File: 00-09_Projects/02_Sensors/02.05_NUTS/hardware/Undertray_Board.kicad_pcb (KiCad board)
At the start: 4 copper layers, 39.6 x 47.7 mm, 95 parts, among them J1 USB_C_Receptacle_USB2.0_16P, J2 Conn_01x04_Socket, J3 Conn_01x06_Pin, J4 SHF-107-01-L-D-SM, SW1 450404015514, SW2 TL3301EF160QG, U1 SN65HVD230, U2 AP2210K-3.3TRG1, U3 STM32F302C8Tx, U4 74HC2G32DP, U5 ASM330LHBTR, U6 VL53L4CDV0DH/1, Y1 RH100-16.000-9-1010-TR

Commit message: LED labels
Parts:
- added kibuzzard-6AD3F554: G***, kibuzzard-6AD3F554, F.Cu at (133.8, 74.9)
- added kibuzzard-6AD3F574: G***, kibuzzard-6AD3F574, F.Cu at (134.2, 80.6)
- added kibuzzard-6AD3F58A: G***, kibuzzard-6AD3F58A, F.Cu at (156.3, 56.8)
- added kibuzzard-6AD3F6DB: G***, kibuzzard-6AD3F6DB, F.Cu at (131.5, 77.6)

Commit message: extra changes
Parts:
- removed kibuzzard-6AD3F554: G***, kibuzzard-6AD3F554
- removed kibuzzard-6AD3F574: G***, kibuzzard-6AD3F574
- removed kibuzzard-6AD3F58A: G***, kibuzzard-6AD3F58A
- removed kibuzzard-6AD3F6DB: G***, kibuzzard-6AD3F6DB
- added C23: 0.1uF, Capacitor_SMD:C_0603_1608Metric_Pad1.08x0.95mm_HandSolder, F.Cu at (139.6, 82.8)
- added R19: 47k, Resistor_SMD:R_0402_1005Metric_Pad0.72x0.64mm_HandSolder, F.Cu at (141.8, 81.6)
- moved C16 3.98 mm to (135.9, 82.0), turned to 180 degrees
- moved D7 2.53 mm to (133.6, 82.9)
- moved R8 2.08 mm to (135.9, 83.6), turned to 180 degrees
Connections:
- U4 pad 2: BOOT0_TRIG -> Net-(C23-Pad1)
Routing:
- net Net-(C23-Pad1): track 0.00 -> 3.39 mm
- net BOOT0_SW: track 3.21 -> 5.41 mm
- net GND: track 32.8 -> 34.8 mm, vias 45 -> 44
- net Net-(D7-K): track 4.47 -> 6.12 mm
- net BOOT0_TRIG: track 9.74 -> 10.5 mm

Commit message: extra changes
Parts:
- R10, R5, R6, R9: value 220 -> 330
- R12: value 100 -> 200
- R13, R16: value 22 -> 47
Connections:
- J4 pad 08: SWO -> unconnected-(J4-Pad08)
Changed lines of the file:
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@@
 			)
 		)
-		(property "Value" "220"
+		(property "Value" "330"
 			(at 0 1.43 0)
 			(layer "F.Fab")
@@
 			)
 		)
-		(property "Value" "220"
+		(property "Value" "330"
 			(at 0 1.43 0)
 			(layer "F.Fab")
@@
 		(sheetname "/MCU/")
 		(sheetfile "mcu.kicad_sch")
+		(units
+			(unit
+				(name "A")
+				(pins "2" "4" "5" "6" "7" "3" "1")
+			)
+		)
 		(attr smd)
 		(duplicate_pad_numbers_are_jumpers no)
@@
 			)
 		)
-		(property "Value" "22"
+		(property "Value" "47"
 			(at 0 1.43 0)
 			(layer "F.Fab")
@@
 			(size 0.74 2.795)
 			(layers "F.Cu" "F.Mask" "F.Paste")
-			(net "SWO")
+			(net "unconnected-(J4-Pad08)")
 			(pinfunction "08_08")
-			(pintype "passive")
+			(pintype "passive+no_connect")
 			(solder_mask_margin 0.102)
 		)
@@
 			)
 		)
-		(property "Value" "22"
+		(property "Value" "47"
 			(at 0 1.43 0)
 			(layer "F.Fab")
@@
 			)
 		)
-		(property "Value" "220"
+		(property "Value" "330"
 			(at 0 1.43 0)
 			(layer "F.Fab")
@@
 			)
 		)
-		(property "Value" "220"
+		(property "Value" "330"
 			(at 0 1.43 90)
 			(layer "F.Fab")
@@
 			)
 		)
-		(property "Value" "100"
+		(property "Value" "200"
 			(at 0 1.43 0)
 			(layer "F.Fab")
@@
 	)
 	(segment
+		(start 140.475 80.8725)
+		(end 141.2025 81.6)
+		(width 0.3)
+		(layer "F.Cu")
+		(net "Net-(C23-Pad1)")
+	)
+	(segment
+		(start 140.865 81.9375)
+		(end 141.2025 81.6)
+		(width 0.3)
+		(layer "F.Cu")
+		(net "Net-(C23-Pad1)")
+	)
+	(segment
+		(start 139.6 81.9375)
+		(end 140.865 81.9375)
+		(width 0.3)
+		(layer "F.Cu")
+		(net "Net-(C23-Pad1)")
+	)
+	(segment
+		(start 140.475 80.25)
+		(end 140.475 80.8725)
+		(width 0.3)
+		(layer "F.Cu")
+		(net "Net-(C23-Pad1)")
+	)
+	(segment
 		(start 136.8 82)
 		(end 138.55 80.25)
@@
 		(net "Net-(U2-BYP{slash}ADJ)")
 	)
-	(segment
-		(start 140.475 80.8725)
-		(end 141.2025 81.6)
-		(width 0.3)
-		(layer "F.Cu")
-		(net "Net-(C23-Pad1)")
-	)
-	(segment
-		(start 140.865 81.9375)
-		(end 141.2025 81.6)
-		(width 0.3)
-		(layer "F.Cu")
-		(net "Net-(C23-Pad1)")
-	)
-	(segment
-		(start 139.6 81.9375)
-		(end 140.865 81.9375)
-		(width 0.3)
-		(layer "F.Cu")
-		(net "Net-(C23-Pad1)")
-	)
-	(segment
-		(start 140.475 80.25)
-		(end 140.475 80.8725)
-		(width 0.3)
-		(layer "F.Cu")
-		(net "Net-(C23-Pad1)")
-	)
 	(zone

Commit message: solder jumper for reset
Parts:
- added JP3: SolderJumper_2_Open, Jumper:SolderJumper-2_P1.3mm_Open_TrianglePad1.0x1.5mm, F.Cu at (130.8, 77.8)
- D3: value RB520S30T5G -> SDM20U30-7
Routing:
- net BOOT0: track 11.2 -> 18.8 mm
- net BOOT0_SW: track 5.41 -> 12.8 mm
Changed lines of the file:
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@@
 		(tags "resistor handsolder")
 		(property "Reference" "R5"
-			(at -0.025 1.5 0)
+			(at 2.7875 0 0)
 			(layer "F.SilkS")
 			(effects
@@
 		)
 	)
+	(footprint "Jumper:SolderJumper-2_P1.3mm_Open_TrianglePad1.0x1.5mm"
+		(layer "F.Cu")
+		(at 130.8 77.775 -90)
+		(descr "SMD Solder Jumper, 1x1.5mm Triangular Pads, 0.3mm gap, open")
+		(tags "solder jumper open")
+		(property "Reference" "JP3"
+			(at -0.775 -2 90)
+			(layer "F.SilkS")
+			(effects
+				(font
+					(size 1 1)
+					(thickness 0.15)
+				)
+			)
+		)
+		(property "Value" "SolderJumper_2_Open"
+			(at 0 1.9 90)
+			(layer "F.Fab")
+			(effects
+				(font
+					(size 1 1)
+					(thickness 0.15)
+				)
+			)
+		)
+		(property "Datasheet" ""
+			(at 0 0 270)
+			(unlocked yes)
+			(layer "F.Fab")
+			(hide yes)
+			(effects
+				(font
+					(size 1.27 1.27)
+					(thickness 0.15)
+				)
+			)
+		)
+		(property "Description" "Solder Jumper, 2-pole, open"
+			(at 0 0 270)
+			(unlocked yes)
+			(layer "F.Fab")
+			(hide yes)
+			(effects
+				(font
+					(size 1.27 1.27)
+					(thickness 0.15)
+				)
+			)
+		)
+		(property ki_fp_filters "SolderJumper*Open*")
+		(sheetname "/MCU/")
+		(sheetfile "mcu.kicad_sch")
+		(units
+			(unit
+				(name "A")
+				(pins "1" "2")
+			)
+		)
+		(zone_connect 1)
+		(attr exclude_from_bom allow_soldermask_bridges)
+		(duplicate_pad_numbers_are_jumpers no)
+		(fp_rect
+			(start -1.225 -0.75)
+			(end 1.225 0.75)
+			(stroke
+				(width 0)
+				(type default)
+			)
+			(fill yes)
+			(layer "F.Mask")
+		)
+		(fp_line
+			(start -1.4 1)
+			(end -1.4 -1)
+			(stroke
+				(width 0.12)
+				(type solid)
+			)
+			(layer "F.SilkS")
+		)
+		(fp_line
+			(start 1.4 1)
+			(end -1.4 1)
+			(stroke
+				(width 0.12)
+				(type solid)
+			)
+			(layer "F.SilkS")
+		)
+		(fp_line
+			(start -1.4 -1)
+			(end 1.4 -1)
+			(stroke
+				(width 0.12)
+				(type solid)
+			)
+			(layer "F.SilkS")
+		)
+		(fp_line
+			(start 1.4 -1)
+			(end 1.4 1)
+			(stroke
+				(width 0.12)
+				(type solid)
+			)
+			(layer "F.SilkS")
+		)
+		(fp_line
+			(start 1.65 1.25)
+			(end -1.65 1.25)
+			(stroke
+				(width 0.05)
+				(type solid)
+			)
+			(layer "F.CrtYd")
+		)
+		(fp_line
+			(start 1.65 1.25)
+			(end 1.65 -1.25)
+			(stroke
+				(width 0.05)
+				(type solid)
+			)
+			(layer "F.CrtYd")
+		)
+		(fp_line
+			(start -1.65 -1.25)
+			(end -1.65 1.25)
+			(stroke
+				(width 0.05)
+				(type solid)
+			)
+			(layer "F.CrtYd")
+		)
+		(fp_line
+			(start -1.65 -1.25)
+			(end 1.65 -1.25)
+			(stroke
+				(width 0.05)
+				(type solid)
+			)
+			(layer "F.CrtYd")
+		)
+		(pad "1" smd custom
+			(at -0.725 0 270)
+			(size 0.3 0.3)
+			(layers "F.Cu" "F.Mask")
+			(net "BOOT0")
+			(pinfunction "A_1")
+			(pintype "passive")
+			(zone_connect 2)
+			(thermal_bridge_angle 45)
+			(options
+				(clearance outline)
+				(anchor rect)
+			)
+			(primitives
+				(gr_poly
+					(pts
+						(xy 1 0) (xy 0.5 0.75) (xy -0.5 0.75) (xy -0.5 -0.75) (xy 0.5 -0.75)
+					)
+					(width 0)
+					(fill yes)
+				)
+			)
+		)
+		(pad "2" smd custom
+			(at 0.725 0 270)
+			(size 0.3 0.3)
+			(layers "F.Cu" "F.Mask")
+			(net "BOOT0_SW")
+			(pinfunction "B_2")
+			(pintype "passive")
+			(zone_connect 2)
+			(thermal_bridge_angle 45)
+			(options
+				(clearance outline)
+				(anchor rect)
+			)
+			(primitives
+				(gr_poly
+					(pts
+						(xy 0.5 0.75) (xy -0.65 0.75) (xy -0.15 0) (xy -0.65 -0.75) (xy 0.5 -0.75)
+					)
+					(width 0)
+					(fill yes)
+				)
+			)
+		)
+		(embedded_fonts no)
+	)
 	(footprint "Resistor_SMD:R_0603_1608Metric_Pad0.98x0.95mm_HandSolder"
 		(layer "F.Cu")
@@
 			)
 		)
-		(property "Value" "RB520S30T5G"
+		(property "Value" "SDM20U30-7"
 			(at 0 -1.4 0)
 			(layer "B.Fab")
@@
 	)
 	(segment
+		(start 137.2 76.825)
+		(end 137.975 77.6)
+		(width 0.2)
+		(layer "F.Cu")
+		(net "BOOT0")
+	)
+	(segment
+		(start 131.025 76.825)
+		(end 137.2 76.825)
+		(width 0.2)
+		(layer "F.Cu")
+		(net "BOOT0")
+	)
+	(segment
 		(start 140.475 75.1)
 		(end 140.475 75.95)
@@
 	)
 	(segment
+		(start 130.8 77.05)
+		(end 131.025 76.825)
+		(width 0.2)
+		(layer "F.Cu")
+		(net "BOOT0")
+	)
+	(segment
 		(start 128.5875 74.9)
 		(end 130.2 74.9)
@@
 	(segment
 		(start 136.7625 82)
+		(end 133.2625 78.5)
+		(width 0.3)
+		(layer "F.Cu")
+		(net "BOOT0_SW")
+	)
+	(segment
+		(start 136.7625 82)
 		(end 136.7625 83.55)
 		(width 0.3)
@@
 		(width 0.3)
 		(layer "F.Cu")
+		(net "BOOT0_SW")
+	)
+	(segment
+		(start 133.2625 78.5)
+		(end 130.8 78.5)
+		(width 0.3)
+		(layer "F.Cu")

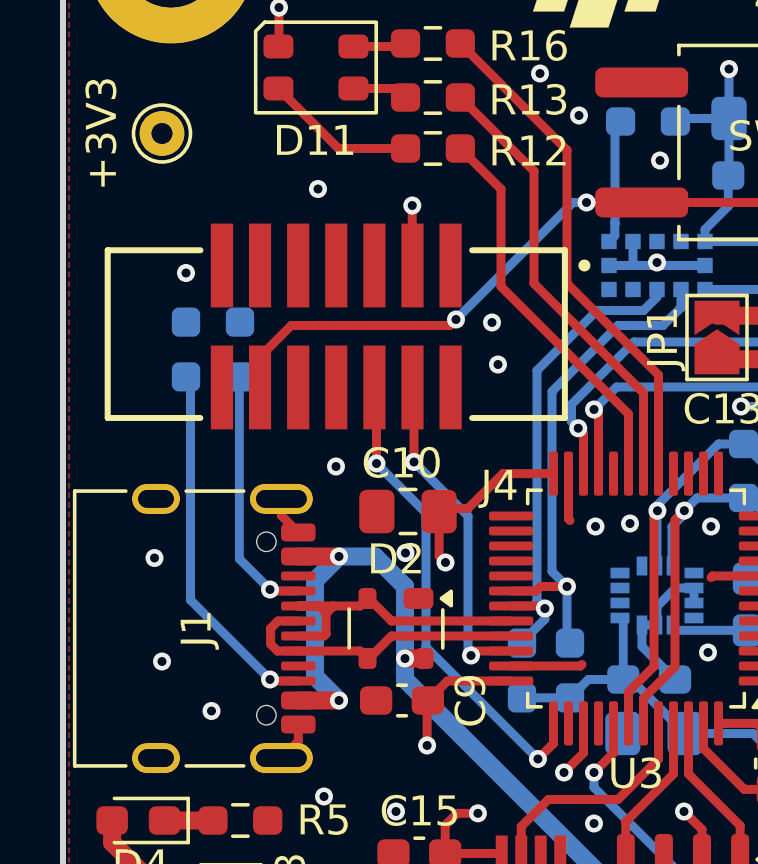
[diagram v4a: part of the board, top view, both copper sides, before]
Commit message: usb D+ pull up res fix
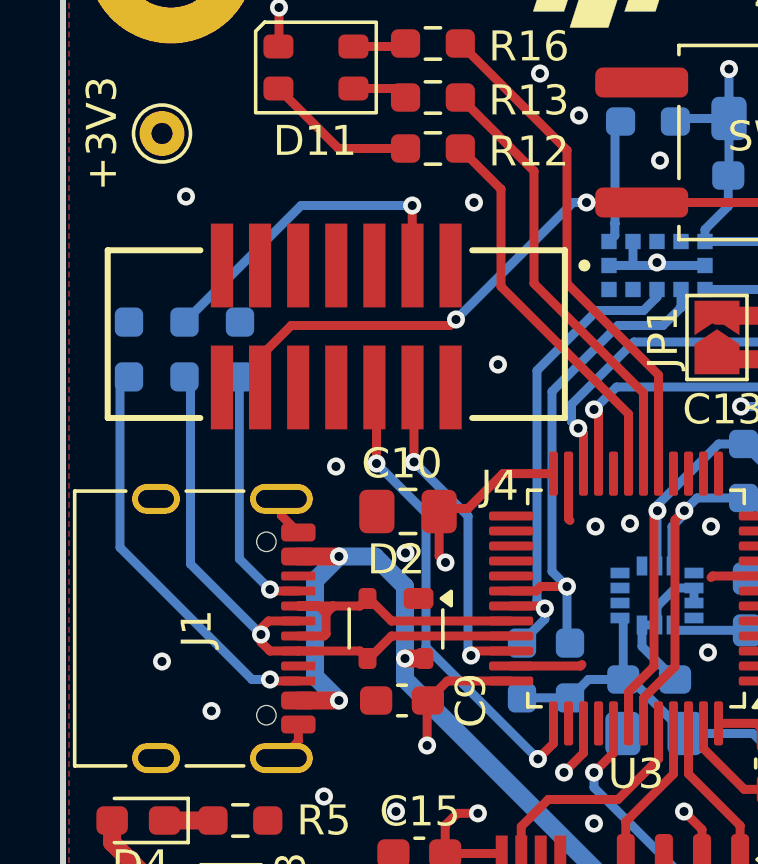
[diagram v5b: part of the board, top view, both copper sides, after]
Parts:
- added R20: 1.5k, Resistor_SMD:R_0603_1608Metric_Pad0.98x0.95mm_HandSolder, B.Cu at (129.2, 59.2)
- moved R2 1.90 mm to (127.4, 59.2)
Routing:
- net USB+: track 10.1 -> 20.3 mm, vias 0 -> 1
- net +3V3: track 85.0 -> 94.2 mm
- net Net-(J1-CC2): track 12.2 -> 13.6 mm
- net GND: vias 44 -> 42
